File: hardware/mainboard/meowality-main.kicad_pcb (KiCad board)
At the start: 6 copper layers, 200 x 75 mm, 266 parts, among them J1 Micro_SD_Card_Det, J2 MINI_DP_SINK, J3 DEBUG, J4 USB_C_Receptacle, J5 Conn_01x02, J6 Conn_01x02, P1 M2_SOCKET_E, Q1 BSS138, Q10 BSS138, Q2 BSS138, Q3 BSS138, Q5 BSS138, Q7 BSS138, SW1 SW_DIP_x04, SW2 SW_Push, SW3 SW_Push, SW4 SW_Push, SW5 SW_Push, SW6 SW_Push, U1 CP3225-100.000-3.3-25-X-T-TR, U10 MMC5983MA, U11 Si52112-B, U12 TPD4E02B04DQA, U13 TPD4E02B04DQA, U14 CBTL02043A, U15 FUSB302B11MPX, U16 USB3318, U17 AP6230xWU, U19 ADP5070ACPZ, U2 AX3HAF1-135.0000T, U20 CAT4106HV4, U21 74LVC2T45DC, U3 AP6230xWU, U4 AP6230xWU, U5 SiC438, U6 AP6230xWU, U7 AP6230xWU, U8 TXS02612, U9 ICM-20789, X1 831056169, Y1 25MHz

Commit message: Initial power routing
Signed-off-by: gatecat <gatecat@ds0.me>
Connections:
- SOM1 pad 2A58: PL_LED4R -> PL_LED2R
- SOM1 pad 2B52: PL_LED2R -> PL_LED4R
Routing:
- net +3V3PS: track 0.00 -> 317.8 mm, vias 0 -> 1
- net +1V8PL: track 2.36 -> 259.3 mm, vias 1 -> 3
- net +5V: track 63.4 -> 295.8 mm, vias 0 -> 4
- net +3V3PL: track 0.00 -> 218.7 mm, vias 0 -> 1
- net PL_LED4R: track 0.51 -> 205.8 mm, vias 1 -> 2
- net +1V8PS: track 0.00 -> 163.0 mm, vias 0 -> 1
- net +1V2PL: track 1.08 -> 129.1 mm, vias 2 -> 3
- net /LCDs&Cams/LCD_AVdd: track 5.61 -> 124.3 mm, vias 1 -> 5
- net /LCDs&Cams/LCD_AVee: track 8.23 -> 126.8 mm, vias 1 -> 5
- net PL_LED2G: track 0.00 -> 15.2 mm, vias 0 -> 1
- net PL_LED2B: track 0.00 -> 14.2 mm, vias 0 -> 1
- net PL_LED1R: track 0.00 -> 13.2 mm, vias 0 -> 1
- net PL_LED3R: track 0.00 -> 11.7 mm, vias 0 -> 1
- net PL_LED3G: track 0.00 -> 11.3 mm, vias 0 -> 1
- net PL_LED3B: track 0.00 -> 11.0 mm, vias 0 -> 1
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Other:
- outline, holes or cut-outs redrawn

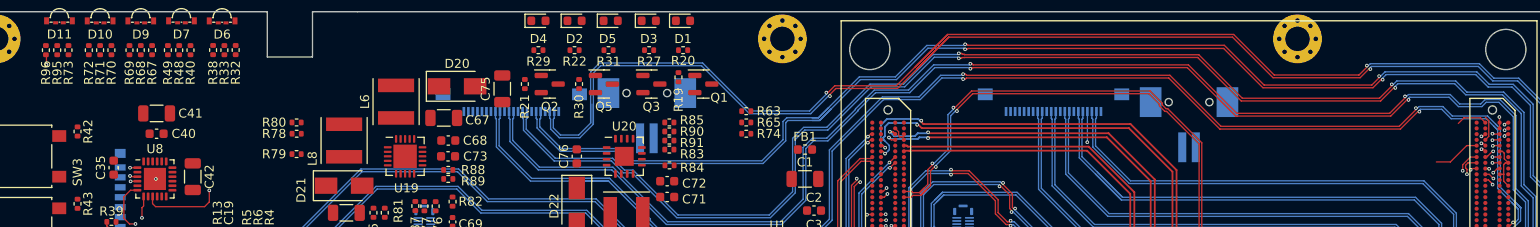
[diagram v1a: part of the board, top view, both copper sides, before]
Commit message: Route and pinswap PL LEDs
Signed-off-by: gatecat <gatecat@ds0.me>
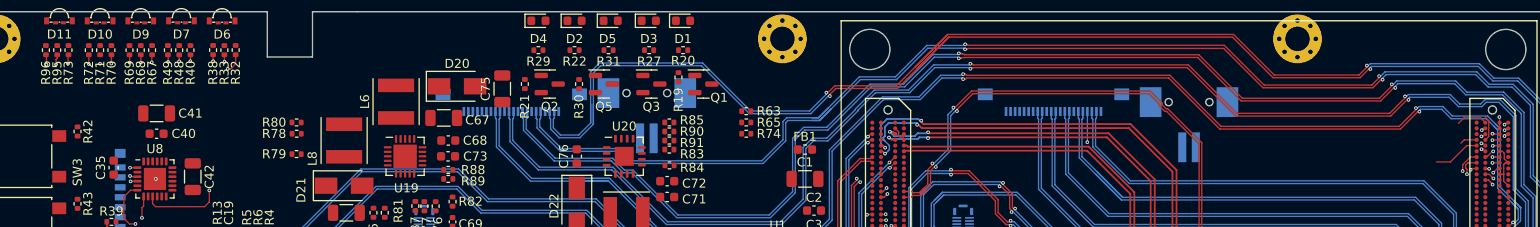
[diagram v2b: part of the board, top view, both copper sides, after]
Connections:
- SOM1 pad 2A58: PL_LED2R -> PL_LED2G
- SOM1 pad 2A59: PL_LED4G -> PL_LED2B
- SOM1 pad 2A60: PL_LED4B -> PL_LED1R
- SOM1 pad 2B53: PL_LED2G -> PL_LED4G
- SOM1 pad 2B54: PL_LED2B -> PL_LED4B
- SOM1 pad 2B56: PL_LED3R -> PL_LED3G
- SOM1 pad 2B57: PL_LED3G -> PL_LED3B
- SOM1 pad 2B58: PL_LED3B -> PL_LED2R
- SOM1 pad 2C54: PL_LED1R -> PL_LED3R
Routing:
- net PL_LED4G: track 6.51 -> 203.7 mm, vias 1 -> 2
- net PL_LED4B: track 5.12 -> 201.0 mm, vias 1 -> 2
- net PL_LED3R: track 11.7 -> 197.2 mm, vias 1 -> 2
- net PL_LED3G: track 11.3 -> 193.8 mm, vias 1 -> 2
- net PL_LED2R: track 7.79 -> 189.5 mm, vias 1 -> 2
- net PL_LED3B: track 11.0 -> 192.6 mm, vias 1 -> 2
- net PL_LED1G: track 0.52 -> 177.8 mm, vias 1 -> 2
- net PL_LED1B: track 0.54 -> 175.8 mm, vias 1 -> 2
- net PL_LED0R: track 0.72 -> 173.6 mm, vias 1 -> 2
- net PL_LED2G: track 15.2 -> 184.7 mm, vias 1 -> 2
- net PL_LED2B: track 14.2 -> 181.6 mm, vias 1 -> 2
- net PL_LED0G: track 2.39 -> 168.7 mm, vias 1 -> 2
- net PL_LED0B: track 2.57 -> 168.5 mm, vias 1 -> 2
- net PL_LED1R: track 13.2 -> 178.4 mm, vias 1 -> 2
- net CAM_L_SCL: track 0.00 -> 6.08 mm, vias 0 -> 1
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
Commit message: Tidy up power routes
Signed-off-by: gatecat <gatecat@ds0.me>
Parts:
- turned D12 to 90 degrees
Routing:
- net CAM_CLK_L: track 1.25 -> 125.8 mm, vias 1 -> 3
- net CAM_PWR_EN: track 0.00 -> 105.9 mm, vias 0 -> 3
- net CAM_R_SDA: track 5.20 -> 105.4 mm, vias 0 -> 5
- net CAM_R_SCL: track 1.90 -> 100.0 mm, vias 0 -> 5
- net UART_RX: track 17.5 -> 108.1 mm, vias 1 -> 4
- net SYS_RESET: track 32.8 -> 116.4 mm, vias 1 -> 2
- net /LCDs&Cams/LCD_LED4-: track 0.00 -> 70.3 mm, vias 0 -> 2
- net /LCDs&Cams/LCD_LED3-: track 0.00 -> 68.0 mm, vias 0 -> 2
- net /LCDs&Cams/LCD_LED+: track 0.00 -> 57.7 mm, vias 0 -> 2
- net CAM_CLK_R: track 1.09 -> 41.3 mm, vias 1 -> 3
- net /LCDs&Cams/LCD_AVee: track 126.8 -> 97.4 mm, vias 5 -> 2
- net /LCDs&Cams/LCD_AVdd: track 124.3 -> 95.1 mm, vias 5 -> 2
- net VBUS: track 0.00 -> 15.0 mm
- net Net-(L3-Pad1): track 0.00 -> 12.7 mm
- net RECOVERY: track 8.14 -> 20.0 mm
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
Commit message: Misc routing
Signed-off-by: gatecat <gatecat@ds0.me>
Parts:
- moved R66 67.0 mm to (87.0, 68.2)
- moved R64 66.9 mm to (87.0, 67.0)
- moved F1 1.77 mm to (58.5, 120.0)
- moved R92 1.75 mm to (96.0, 90.8)
- moved R94 1.25 mm to (96.0, 89.2)
- moved D12 0.75 mm to (63.0, 121.2)
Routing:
- net DP_AUX-: track 0.00 -> 217.9 mm, vias 0 -> 5
- net DP_HPD: track 3.46 -> 220.1 mm, vias 0 -> 1
- net DP_AUX+: track 0.00 -> 213.9 mm, vias 0 -> 5
- net LEFT_LCD_TE: track 0.00 -> 188.6 mm, vias 0 -> 3
- net LEFT_LCD_~{RST}: track 0.00 -> 183.6 mm, vias 0 -> 5
- net MAG_SCL: track 0.00 -> 151.5 mm, vias 0 -> 7
- net IMU_FSYNC: track 0.00 -> 151.4 mm, vias 0 -> 4
- net MAG_SDA: track 0.00 -> 148.0 mm, vias 0 -> 5
- net IMU_INT: track 0.00 -> 127.8 mm, vias 0 -> 4
- net BTN2: track 0.00 -> 116.1 mm, vias 0 -> 2
- net BTN3: track 0.00 -> 114.5 mm, vias 0 -> 2
- net BTN1: track 0.00 -> 107.5 mm, vias 0 -> 2
- net BTN0: track 0.00 -> 99.0 mm, vias 0 -> 2
- net PD_INT: track 17.0 -> 111.6 mm, vias 2 -> 4
- net CAM_R_SCL: track 100.0 -> 175.8 mm, vias 5 -> 6
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
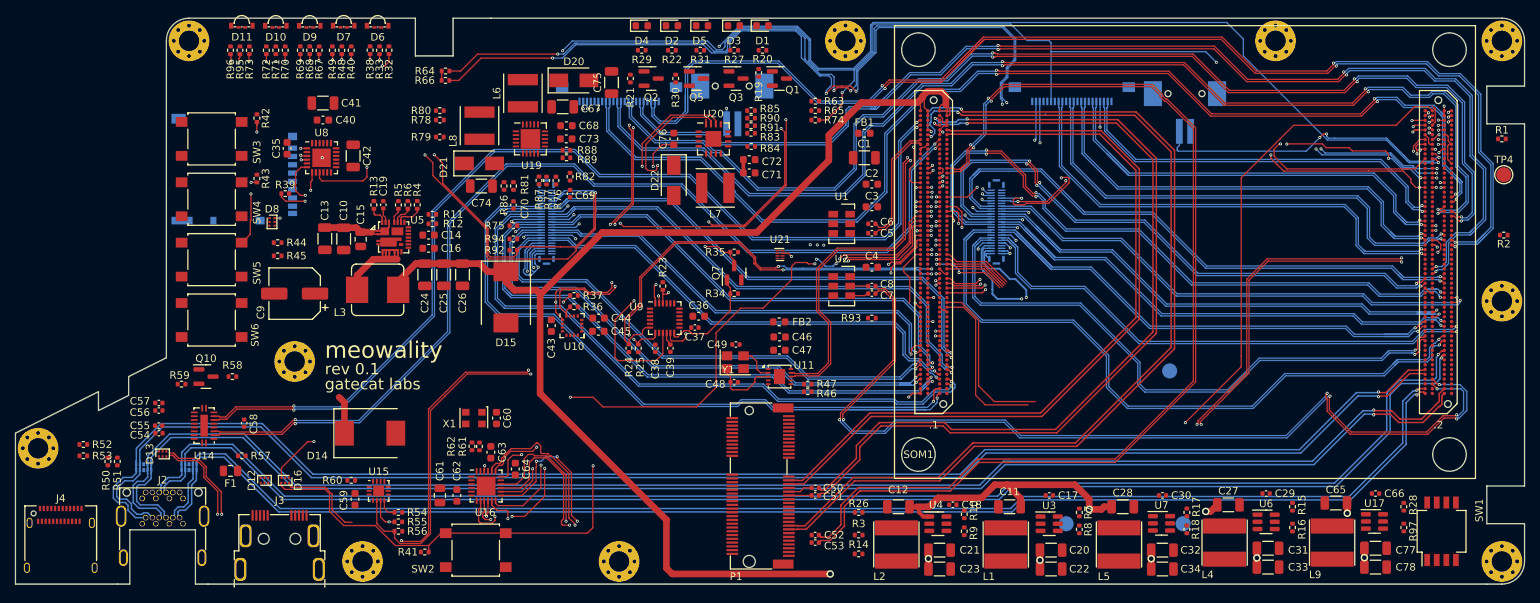
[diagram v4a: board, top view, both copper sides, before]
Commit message: Debug signal pinswaps and routing
Signed-off-by: gatecat <gatecat@ds0.me>
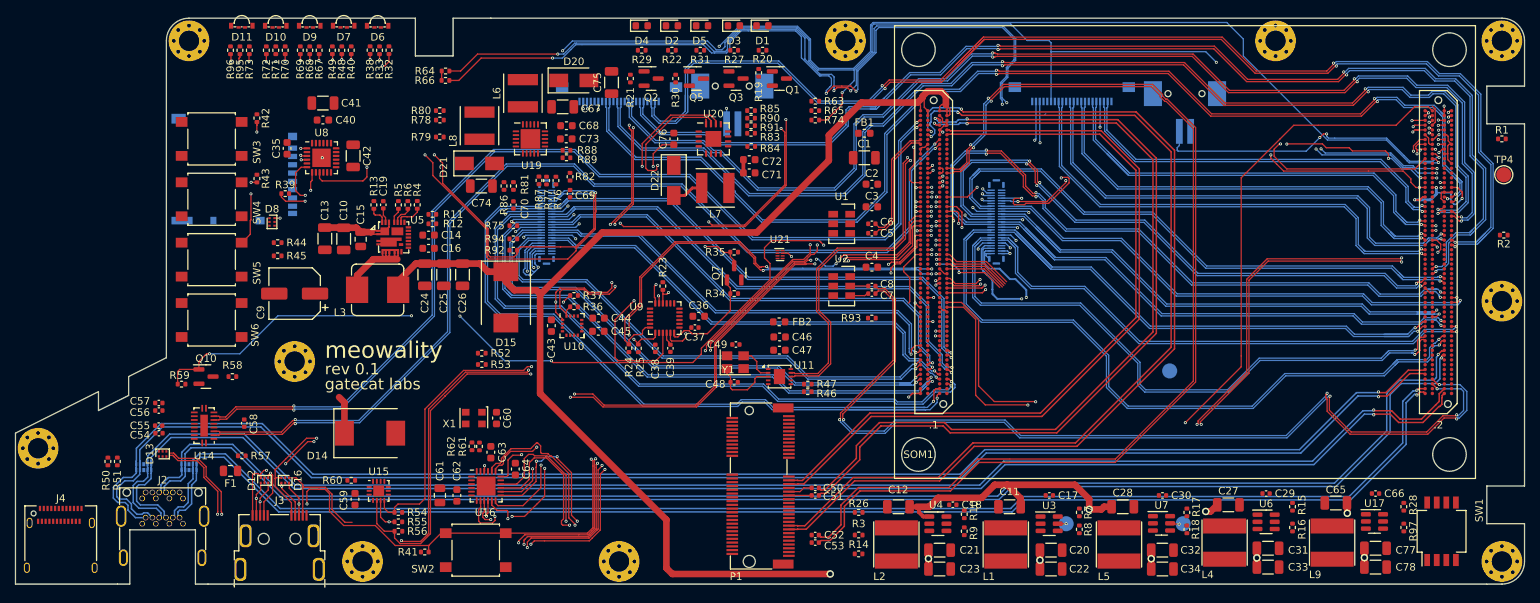
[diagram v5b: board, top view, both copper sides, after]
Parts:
- moved R53 54.2 mm to (91.8, 105.9)
- moved R52 54.2 mm to (91.8, 104.4)
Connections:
- D12 pad 1: JTAG_TDI -> JTAG_TMS
- D12 pad 4: JTAG_TMS -> JTAG_TDI
- D16 pad 1: UART_TX -> RECOVERY
- D16 pad 3: UART_RX -> UART_TX
- D16 pad 4: SYS_RESET -> UART_RX
- D16 pad 6: RECOVERY -> SYS_RESET
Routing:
- net JTAG_TCK: track 38.1 -> 148.4 mm, vias 1 -> 4
- net JTAG_TMS: track 33.7 -> 143.8 mm, vias 1 -> 4
- net JTAG_TDO: track 35.2 -> 144.7 mm, vias 1 -> 4
- net JTAG_TDI: track 36.6 -> 145.2 mm, vias 1 -> 4
- net UART_TX: track 7.01 -> 114.9 mm, vias 1 -> 4
- net USBC_SEL: track 15.6 -> 120.0 mm, vias 2 -> 6
- net PD_I2C_SDA: track 20.1 -> 99.6 mm, vias 2 -> 4
- net VccO_EN_PS: track 22.0 -> 77.0 mm, vias 0 -> 2
- net PD_I2C_SCL: track 60.9 -> 107.7 mm, vias 5 -> 6
- net VccO_EN_PL: track 22.3 -> 64.7 mm, vias 0 -> 2
- net +1V2PL: track 131.3 -> 150.3 mm, vias 5 -> 8
- net +1V8PL: track 250.3 -> 256.2 mm
- net SYS_RESET: track 116.4 -> 121.5 mm, vias 2 -> 4
- net UART_RX: track 108.1 -> 112.3 mm, vias 4 -> 6
- net Net-(D22-Pad2): track 0.00 -> 4.11 mm
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
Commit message: USB and other misc routing
Signed-off-by: gatecat <gatecat@ds0.me>
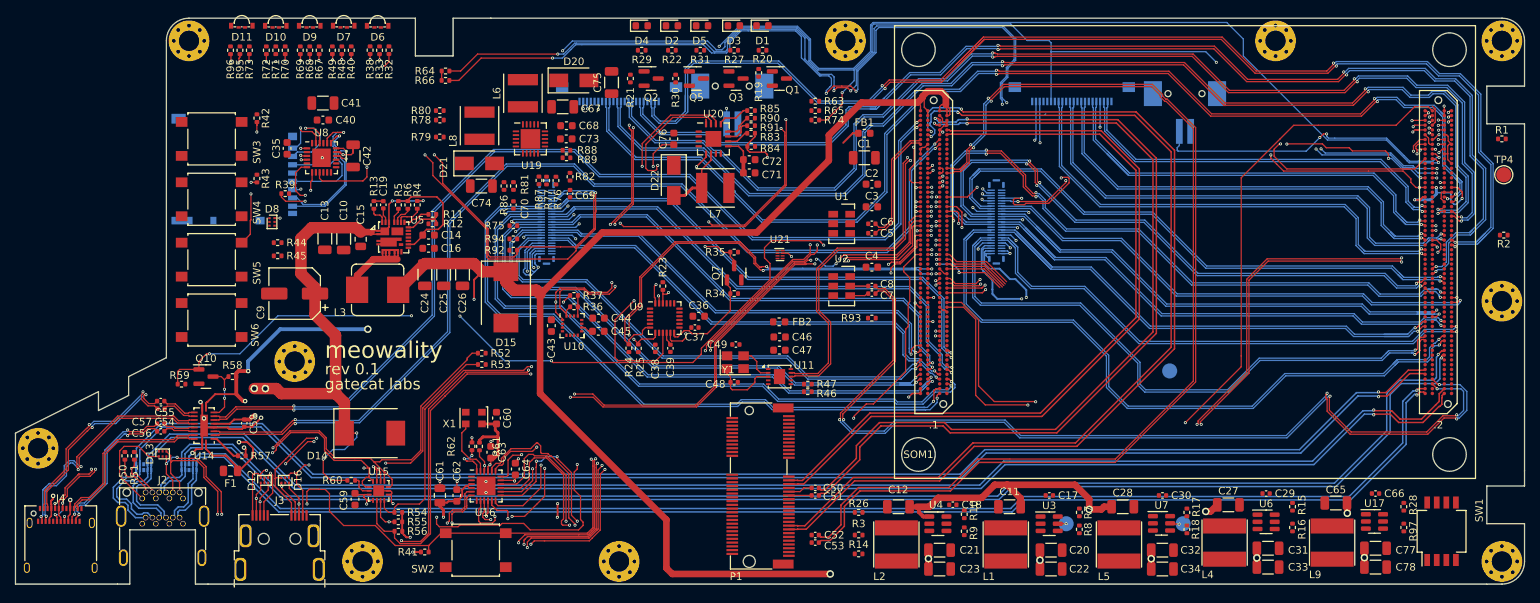
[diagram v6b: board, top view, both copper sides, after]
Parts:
- moved C55 3.26 mm to (49.2, 110.8)
- moved C54 3.26 mm to (49.3, 111.8)
- moved C56 2.76 mm to (49.2, 114.8)
- moved C57 2.76 mm to (49.2, 113.8)
- moved R50 2.37 mm to (44.5, 118.0)
- moved R51 2.37 mm to (45.8, 118.0)
- turned R61 to -90 degrees
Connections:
- U14 pad 12: /IO/SSTXC2- -> /IO/SSTXC1-
- U14 pad 13: /IO/SSTXC2+ -> /IO/SSTXC1+
- U14 pad 14: /IO/SSRX2- -> /IO/SSRX1-
- U14 pad 15: /IO/SSRX2+ -> /IO/SSRX1+
- U14 pad 16: /IO/SSTXC1- -> /IO/SSTXC2-
- U14 pad 17: /IO/SSTXC1+ -> /IO/SSTXC2+
- U14 pad 18: /IO/SSRX1- -> /IO/SSRX2-
- U14 pad 19: /IO/SSRX1+ -> /IO/SSRX2+
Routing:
- net VBUS: track 15.0 -> 128.5 mm, vias 0 -> 8
- net RECOVERY: track 24.1 -> 126.4 mm, vias 0 -> 4
- net /IO/CC2: track 0.00 -> 80.2 mm, vias 0 -> 4
- net /IO/CC1: track 0.00 -> 79.4 mm, vias 0 -> 2
- net USB2_D-: track 0.00 -> 76.9 mm, vias 0 -> 4
- net USB2_D+: track 0.00 -> 75.8 mm, vias 0 -> 2
- net +3V3PS: track 317.8 -> 378.7 mm, vias 1 -> 9
- net +5V: track 300.9 -> 352.3 mm, vias 4 -> 6
- net /IO/SSRX1+: track 0.00 -> 31.8 mm, vias 0 -> 2
- net /IO/SSRX1-: track 0.00 -> 31.6 mm, vias 0 -> 2
- net GND: track 100.3 -> 130.0 mm, vias 25 -> 39
- net /IO/SSTX1+: track 0.00 -> 26.4 mm, vias 0 -> 2
- net /IO/SSTX1-: track 0.00 -> 25.3 mm, vias 0 -> 2
- net /IO/SSRX2-: track 0.00 -> 22.6 mm
- net /IO/SSRX2+: track 0.00 -> 22.1 mm
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
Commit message: Routing various remaining bits
Signed-off-by: gatecat <gatecat@ds0.me>
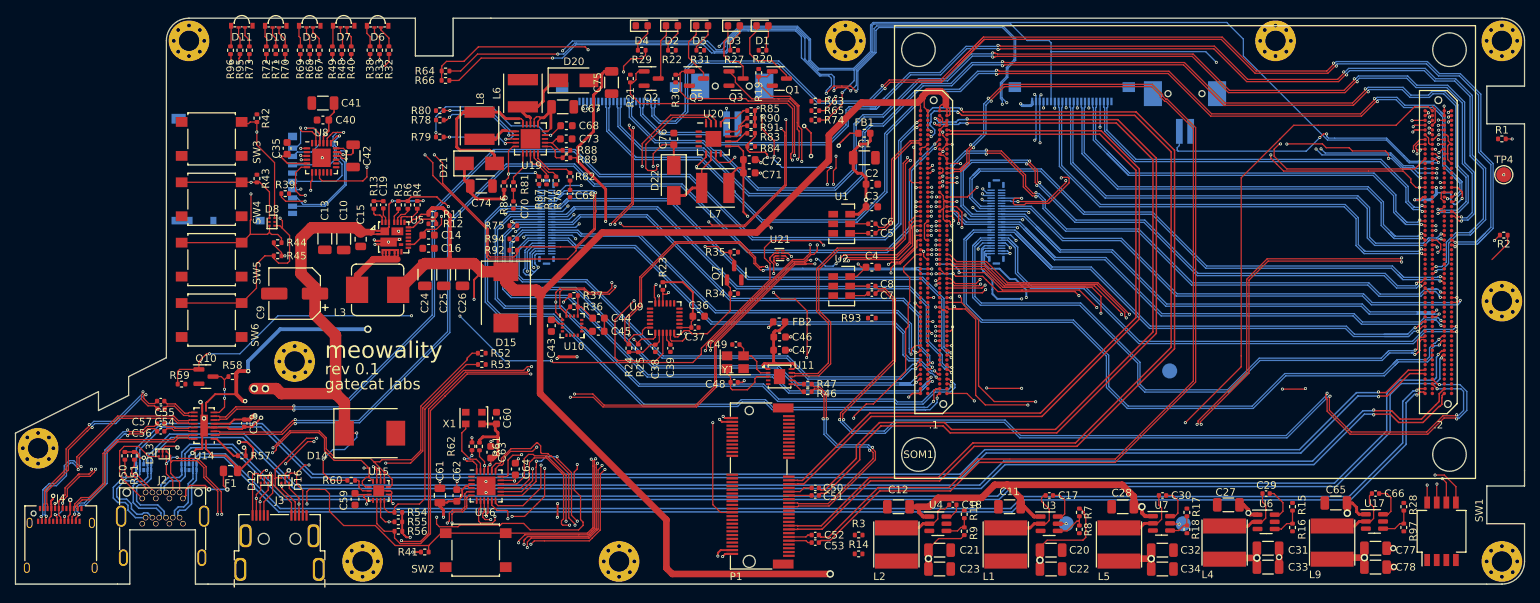
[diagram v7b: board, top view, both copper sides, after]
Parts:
- removed R26: 10k, Resistor_SMD:R_0402_1005Metric
- turned C27 to 180 degrees
- turned C28 to 180 degrees
- turned C29 to 180 degrees
- turned L8 to 90 degrees
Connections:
- D8 pad 1: BTN0 -> BTN1
- D8 pad 2: Net-(D8-Pad2) -> GND
- D8 pad 3: BTN1 -> BTN2
- D8 pad 4: BTN2 -> BTN3
- D8 pad 5: Net-(D8-Pad2) -> GND
- D8 pad 6: BTN3 -> BTN0
- SW3 pad 2: Net-(D8-Pad2) -> GND
- SW4 pad 2: Net-(D8-Pad2) -> GND
- SW5 pad 2: Net-(D8-Pad2) -> GND
- SW6 pad 2: Net-(D8-Pad2) -> GND
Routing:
- net POWEROFF: track 0.67 -> 115.9 mm, vias 1 -> 4
- net Net-(R1-Pad2): track 0.00 -> 115.2 mm, vias 0 -> 6
- net /SOM/PERST_IN: track 10.5 -> 108.3 mm, vias 2 -> 4
- net PS_ERR_OUT: track 0.59 -> 80.7 mm, vias 1 -> 2
- net PS_ERR_STAT: track 0.65 -> 75.9 mm, vias 1 -> 2
- net Net-(SOM1-Pad1A30): track 9.41 -> 82.3 mm, vias 0 -> 2
- net Net-(SOM1-Pad1A29): track 9.09 -> 81.6 mm, vias 0 -> 2
- net Net-(SOM1-Pad1A28): track 8.72 -> 80.2 mm, vias 0 -> 2
- net Net-(SOM1-Pad1A27): track 8.35 -> 79.7 mm, vias 0 -> 2
- net VccO_EN_PS: track 77.0 -> 144.7 mm, vias 2 -> 4
- net VccO_EN_PL: track 64.7 -> 128.3 mm, vias 2 -> 4
- net /Periph/PS_LED_3V3: track 0.00 -> 61.0 mm, vias 0 -> 6
- net GND: track 130.0 -> 187.4 mm, vias 39 -> 79
- net /LCDs&Cams/LCD_LEDPWM: track 0.17 -> 51.4 mm, vias 0 -> 2
- net /LCDs&Cams/LCD_AVee: track 97.4 -> 147.8 mm, vias 2 -> 5
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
